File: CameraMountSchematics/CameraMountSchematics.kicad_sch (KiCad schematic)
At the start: 9 parts, among them M1 Stepper_Motor_bipolar, M2 Motor_Servo, U1 L78L33_TO92, U2 Pico, U3 JDY-08

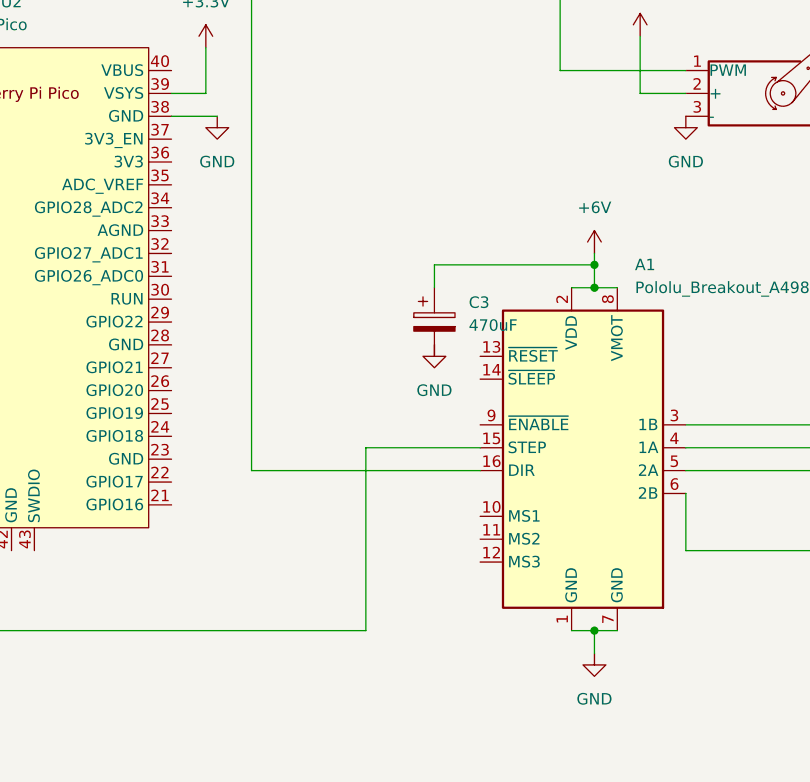
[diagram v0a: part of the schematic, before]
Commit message: 1. Add some  component libraries as submodules 2. Fixing stepper driver logic voltage
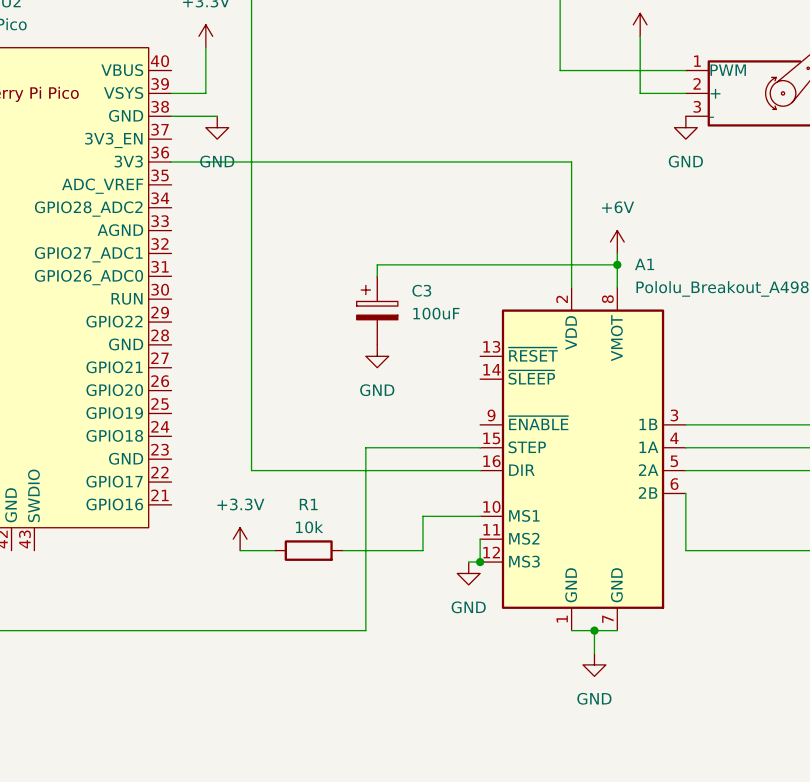
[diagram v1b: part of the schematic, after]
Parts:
- added R1: 10k, symbol Device:R
- C3: value 470uF -> 100uF
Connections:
- net +3.3V: now also R1.1
- net +6V: no longer A1.2 (VDD)
- net GND: now also A1.11 (MS2), A1.12 (MS3), C3.2
- net at A1.10 (MS1): now also R1.2
- net at U2.36 (3V3): now also A1.2 (VDD)
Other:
- company: (none) -> Bogdan Zaiats
- title: (none) -> Camera mount schematic
- moved on the sheet: C3
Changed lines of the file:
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@@
 (kicad_sch (version 20230121) (generator eeschema)
   (paper "A4" portrait)
+  (title_block
+    (title "Camera mount schematic")
+    (date "2023-06-24")
+    (company "Bogdan Zaiats")
+  )
   (junction (at 53.34 60.96) (diameter 0) (color 0 0 0 0)
   )
@@
   (junction (at 135.89 123.19) (diameter 0) (color 0 0 0 0)
   )
-  (junction (at 135.89 82.55) (diameter 0) (color 0 0 0 0)
-  )
-  (junction (at 135.89 85.09) (diameter 0) (color 0 0 0 0)
+  (junction (at 138.43 82.55) (diameter 0) (color 0 0 0 0)
+  )
+  (junction (at 123.19 115.57) (diameter 0) (color 0 0 0 0)
   )
   (junction (at 52.07 26.67) (diameter 0) (color 0 0 0 0)
   )
-  (wire (pts (xy 118.11 82.55) (xy 135.89 82.55))
-    (stroke (width 0) (type default))
-  )
-  (wire (pts (xy 135.89 82.55) (xy 135.89 85.09))
-    (stroke (width 0) (type default))
-  )
-  (wire (pts (xy 135.89 81.28) (xy 135.89 82.55))
+  (wire (pts (xy 138.43 82.55) (xy 138.43 85.09))
+    (stroke (width 0) (type default))
+  )
+  (wire (pts (xy 138.43 81.28) (xy 138.43 82.55))
     (stroke (width 0) (type default))
   )
@@
     (stroke (width 0) (type default))
   )
+  (wire (pts (xy 116.84 114.3) (xy 116.84 110.49))
+    (stroke (width 0) (type default))
+  )
   (wire (pts (xy 140.97 57.15) (xy 140.97 63.5))
     (stroke (width 0) (type default))
@@
     (stroke (width 0) (type default))
   )
-  (wire (pts (xy 118.11 85.09) (xy 118.11 82.55))
+  (wire (pts (xy 111.76 83.82) (xy 111.76 82.55))
     (stroke (width 0) (type default))
   )
@@
     (stroke (width 0) (type default))
   )
-  (wire (pts (xy 135.89 85.09) (xy 138.43 85.09))
+  (wire (pts (xy 88.9 71.12) (xy 133.35 71.12))
+    (stroke (width 0) (type default))
+  )
+  (wire (pts (xy 123.19 113.03) (xy 123.19 115.57))
     (stroke (width 0) (type default))
   )
@@
     (stroke (width 0) (type default))
   )
+  (wire (pts (xy 133.35 71.12) (xy 133.35 85.09))
+    (stroke (width 0) (type default))
+  )
   (wire (pts (xy 132.08 60.96) (xy 146.05 60.96))
     (stroke (width 0) (type default))
   )
+  (wire (pts (xy 121.92 115.57) (xy 123.19 115.57))
+    (stroke (width 0) (type default))
+  )
   (wire (pts (xy 92.71 58.42) (xy 92.71 63.5))
     (stroke (width 0) (type default))
@@
     (stroke (width 0) (type default))
   )
-  (wire (pts (xy 133.35 85.09) (xy 135.89 85.09))
-    (stroke (width 0) (type default))
-  )
   (wire (pts (xy 135.89 125.73) (xy 135.89 123.19))
     (stroke (width 0) (type default))
@@
     (stroke (width 0) (type default))
   )
+  (wire (pts (xy 111.76 82.55) (xy 138.43 82.55))
+    (stroke (width 0) (type default))
+  )
+  (wire (pts (xy 116.84 110.49) (xy 123.19 110.49))
+    (stroke (width 0) (type default))
+  )
   (wire (pts (xy 121.92 144.78) (xy 121.92 186.69))
     (stroke (width 0) (type default))
@@
     (stroke (width 0) (type default))
   )
+  (wire (pts (xy 96.52 114.3) (xy 100.33 114.3))
+    (stroke (width 0) (type default))
+  )
   (wire (pts (xy 160.02 105.41) (xy 160.02 109.22))
     (stroke (width 0) (type default))
@@
     (stroke (width 0) (type default))
   )
+  (wire (pts (xy 107.95 114.3) (xy 116.84 114.3))
+    (stroke (width 0) (type default))
+  )
   (wire (pts (xy 97.79 43.18) (xy 97.79 105.41))
     (stroke (width 0) (type default))
@@
     )
   )
+  (symbol (lib_id "power:+3.3V") (at 96.52 114.3 0) (unit 1)
+    (in_bom yes) (on_board yes) (dnp no)
+    (property "Reference" "#PWR016" (at 96.52 118.11 0)
+      (effects (font (size 1.27 1.27)) hide)
+    )
+    (property "Value" "+3.3V" (at 96.52 109.22 0)
+      (effects (font (size 1.27 1.27)))
+    )
+    (property "Footprint" "" (at 96.52 114.3 0)
+      (effects (font (size 1.27 1.27)) hide)
+    )
+    (property "Datasheet" "" (at 96.52 114.3 0)
+      (effects (font (size 1.27 1.27)) hide)
+    )
+    (pin "1")
+    (instances
+      (project "CameraMountSchematics"
+        (path "/2459aaf8-f4e1-4627-ad4c-a6d0d0db1552"
+          (reference "#PWR016") (unit 1)
+        )
+      )
+    )
+  )
   (symbol (lib_id "power:+3.3V") (at 76.2 156.21 0) (unit 1)
     (in_bom yes) (on_board yes) (dnp no) (fields_autoplaced)
@@
     )
   )
-  (symbol (lib_id "power:GND") (at 118.11 91.44 0) (unit 1)
-    (in_bom yes) (on_board yes) (dnp no) (fields_autoplaced)
-    (property "Reference" "#PWR012" (at 118.11 97.79 0)
-      (effects (font (size 1.27 1.27)) hide)
-    )
-    (property "Value" "GND" (at 118.11 96.52 0)
-      (effects (font (size 1.27 1.27)))
-    )
-    (property "Footprint" "" (at 118.11 91.44 0)
-      (effects (font (size 1.27 1.27)) hide)
-    )
-    (property "Datasheet" "" (at 118.11 91.44 0)
+  (symbol (lib_id "power:GND") (at 111.76 91.44 0) (unit 1)
+    (in_bom yes) (on_board yes) (dnp no) (fields_autoplaced)
+    (property "Reference" "#PWR012" (at 111.76 97.79 0)
+      (effects (font (size 1.27 1.27)) hide)
+    )
+    (property "Value" "GND" (at 111.76 96.52 0)
+      (effects (font (size 1.27 1.27)))
+    )
+    (property "Footprint" "" (at 111.76 91.44 0)
+      (effects (font (size 1.27 1.27)) hide)
+    )
+    (property "Datasheet" "" (at 111.76 91.44 0)
       (effects (font (size 1.27 1.27)) hide)
     )
@@
         (path "/2459aaf8-f4e1-4627-ad4c-a6d0d0db1552"
           (reference "#PWR012") (unit 1)
+        )
+      )
+    )
+  )
+  (symbol (lib_id "Device:R") (at 104.14 114.3 90) (unit 1)
+    (in_bom yes) (on_board yes) (dnp no)
+    (property "Reference" "R1" (at 104.14 109.22 90)
+      (effects (font (size 1.27 1.27)))
+    )
+    (property "Value" "10k" (at 104.14 111.76 90)
+      (effects (font (size 1.27 1.27)))
+    )
+    (property "Footprint" "" (at 104.14 116.078 90)
+      (effects (font (size 1.27 1.27)) hide)
+    )
+    (property "Datasheet" "~" (at 104.14 114.3 0)
+      (effects (font (size 1.27 1.27)) hide)
+    )
+    (pin "1")
+    (pin "2")
+    (instances
+      (project "CameraMountSchematics"
+        (path "/2459aaf8-f4e1-4627-ad4c-a6d0d0db1552"
+          (reference "R1") (unit 1)
         )
       )
@@
     )
   )
-  (symbol (lib_id "power:+6V") (at 135.89 81.28 0) (unit 1)
-    (in_bom yes) (on_board yes) (dnp no) (fields_autoplaced)
-    (property "Reference" "#PWR05" (at 135.89 85.09 0)
-      (effects (font (size 1.27 1.27)) hide)
-    )
-    (property "Value" "+6V" (at 135.89 76.2 0)
-      (effects (font (size 1.27 1.27)))
-    )
-    (property "Footprint" "" (at 135.89 81.28 0)
-      (effects (font (size 1.27 1.27)) hide)
-    )
-    (property "Datasheet" "" (at 135.89 81.28 0)
+  (symbol (lib_id "power:+6V") (at 138.43 81.28 0) (unit 1)
+    (in_bom yes) (on_board yes) (dnp no) (fields_autoplaced)
+    (property "Reference" "#PWR05" (at 138.43 85.09 0)
+      (effects (font (size 1.27 1.27)) hide)
+    )
+    (property "Value" "+6V" (at 138.43 76.2 0)
+      (effects (font (size 1.27 1.27)))
+    )
+    (property "Footprint" "" (at 138.43 81.28 0)
+      (effects (font (size 1.27 1.27)) hide)
+    )
+    (property "Datasheet" "" (at 138.43 81.28 0)
       (effects (font (size 1.27 1.27)) hide)
     )
@@
     )
   )
-  (symbol (lib_id "Device:C_Polarized") (at 118.11 88.9 0) (unit 1)
-    (in_bom yes) (on_board yes) (dnp no) (fields_autoplaced)
-    (property "Reference" "C3" (at 121.92 86.741 0)
-      (effects (font (size 1.27 1.27)) (justify left))
-    )
-    (property "Value" "470uF" (at 121.92 89.281 0)
-      (effects (font (size 1.27 1.27)) (justify left))
-    )
-    (property "Footprint" "" (at 119.0752 92.71 0)
-      (effects (font (size 1.27 1.27)) hide)
-    )
-    (property "Datasheet" "~" (at 118.11 88.9 0)
+  (symbol (lib_id "Device:C_Polarized") (at 111.76 87.63 0) (unit 1)
+    (in_bom yes) (on_board yes) (dnp no) (fields_autoplaced)
+    (property "Reference" "C3" (at 115.57 85.471 0)
+      (effects (font (size 1.27 1.27)) (justify left))
+    )
+    (property "Value" "100uF" (at 115.57 88.011 0)
+      (effects (font (size 1.27 1.27)) (justify left))
+    )
+    (property "Footprint" "" (at 112.7252 91.44 0)
+      (effects (font (size 1.27 1.27)) hide)
+    )
+    (property "Datasheet" "~" (at 111.76 87.63 0)
       (effects (font (size 1.27 1.27)) hide)
     )
@@
         )
       )
+    )
+  )
+  (symbol (lib_id "power:GND") (at 121.92 115.57 0) (unit 1)
+    (in_bom yes) (on_board yes) (dnp no) (fields_autoplaced)
+    (property "Reference" "#PWR015" (at 121.92 121.92 0)
+      (effects (font (size 1.27 1.27)) hide)
+    )
+    (property "Value" "GND" (at 121.92 120.65 0)
+      (effects (font (size 1.27 1.27)))
+    )
+    (property "Footprint" "" (at 121.92 115.57 0)
+      (effects (font (size 1.27 1.27)) hide)
+    )
+    (property "Datasheet" "" (at 121.92 115.57 0)
+      (effects (font (size 1.27 1.27)) hide)
+    )
+    (pin "1")
+    (instances
+      (project "CameraMountSchematics"
+        (path "/2459aaf8-f4e1-4627-ad4c-a6d0d0db1552"
+          (reference "#PWR015") (unit 1)
+        )
+      )

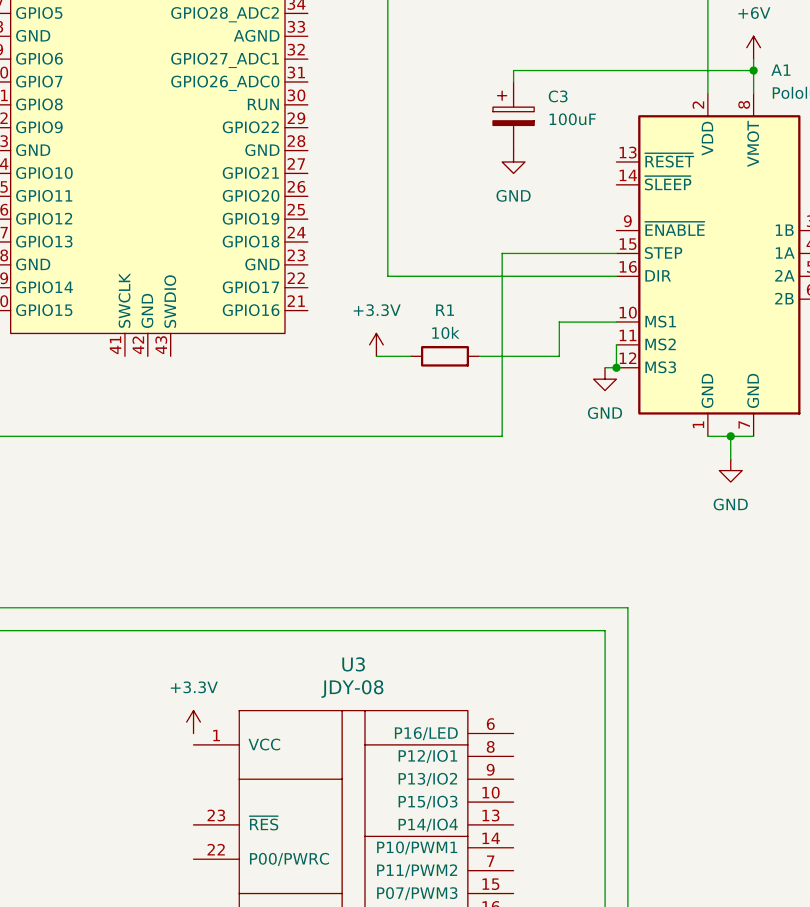
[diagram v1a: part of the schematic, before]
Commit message: fix motor didn`t spin
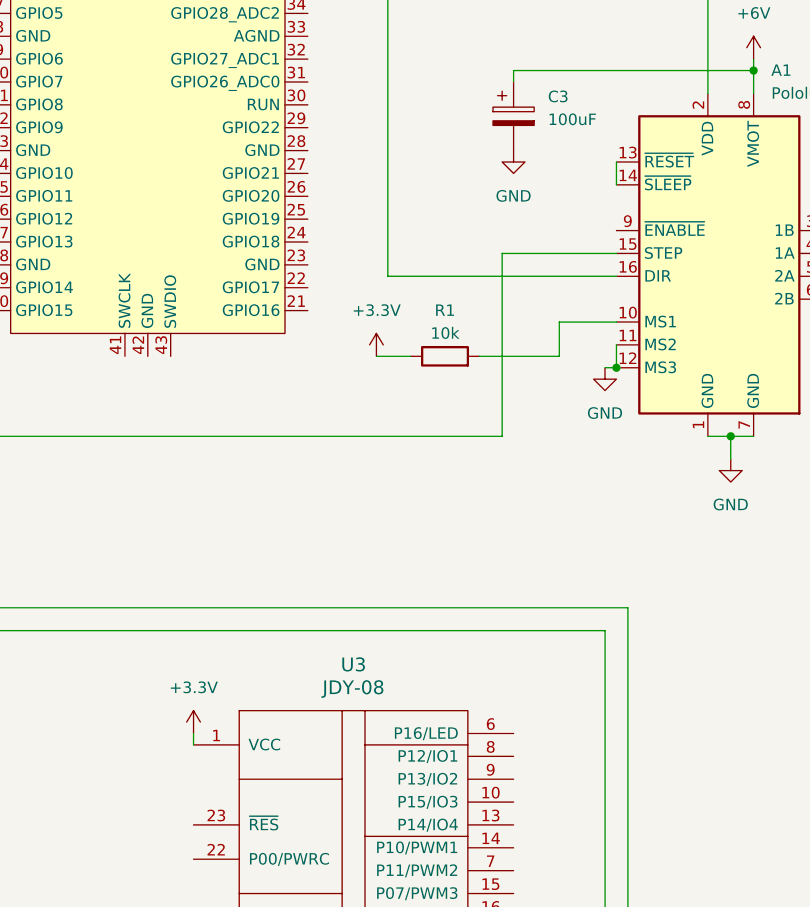
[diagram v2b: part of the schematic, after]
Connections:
- net +3.3V: now also U3.1 (VCC)
- net at A1.13 (~{RESET}): now also A1.14 (~{SLEEP})
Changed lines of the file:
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@@
+    (stroke (width 0) (type default))
+  )
+  (wire (pts (xy 123.19 92.71) (xy 123.19 95.25))
     (stroke (width 0) (type default))
   )
@@
     (stroke (width 0) (type default))
   )
+  (wire (pts (xy 76.2 156.21) (xy 76.2 157.48))
+    (stroke (width 0) (type default))
+  )
